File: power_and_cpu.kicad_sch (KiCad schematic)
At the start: 252 parts, among them J1 CPU1 USB, J10 AUX GPIO 1, J11 CAN2 PLUG, J12 Conn_01x06, J13 ADC AUX 2, J14 AUX GPIO 2, J15 AUX Encoder, J17 CAN Output, J2 CAN Input, J21 Power Input, J3 Encoder 1, J4 Encoder 2, J5 Conn_01x06, J6 CPU2 USB, J7 Conn_01x02, J9 ADC AUX 1, Q7 Q_NMOS_GSD, SW1 SW_MEC_5G, SW2 SW_MEC_5G, SW3 CONFIG SWITCH, U10 TXS0101DCKR, U11 TLV1117LV33DCYR, U12 W25Q128JVSIQ, U13 W25Q128JVSIQ, U15 RP2040, U16 ADC081S021CISD/NOPB, U17 isolator, U18 MCP2515-xSO, U19 RP2040, U23 SN74LVC1G07QDCKTQ1, U24 MT2492, U25 NCP1117-5_SOT223, U26 ADC081S021CISD/NOPB, U27 USBLC6-2P6, U28 USBLC6-2P6, U29 USBLC6-4SC6, U3 USBLC6-4SC6, U30 USBLC6-4SC6, U31 USBLC6-4SC6, U32 TLV1117LV33DCYR, U33 TX4139, U34 LTV-208, U43 USBLC6-4SC6, U6 SN74LVC1G07QDCKTQ1, U9 ADC081S021CISD/NOPB, Y1 12MHz, Y2 12MHz, Y3 16MHz

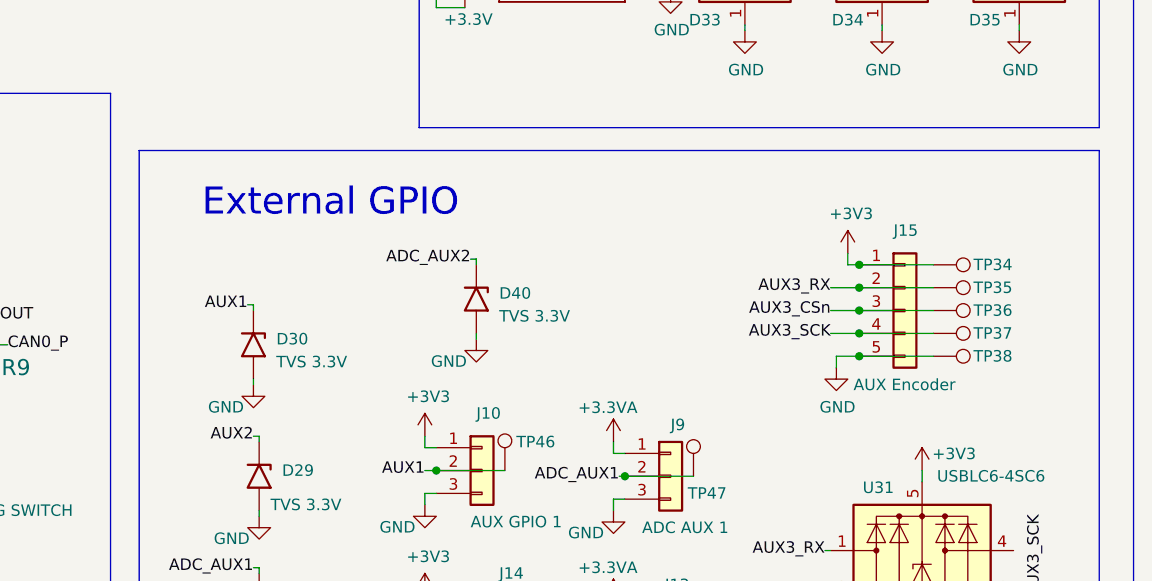
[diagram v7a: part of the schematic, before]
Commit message: Changed current sense circuit as per recommendation. Added extra combined AUX port.
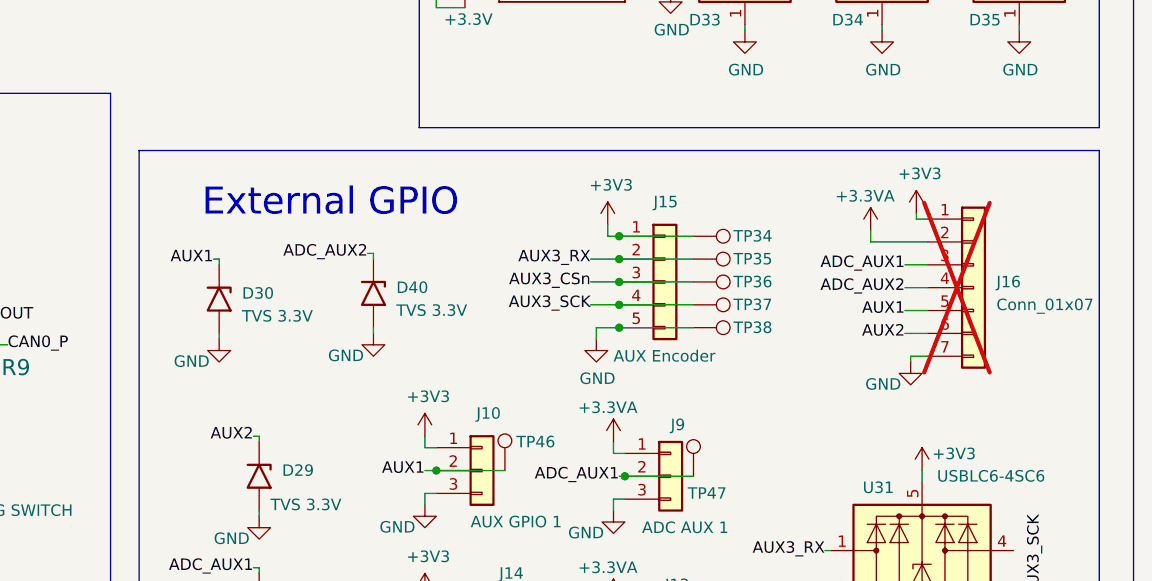
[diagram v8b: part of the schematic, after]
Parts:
- added J16: Conn_01x07, Connector_PinHeader_2.54mm:PinHeader_2x04_P2.54mm_Vertical, symbol Connector_Generic:Conn_01x07
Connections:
- net +3.3VA: now also J16.2 (Pin_2)
- net +3V3: now also J16.1 (Pin_1)
- net ADC_AUX1: now also J16.3 (Pin_3)
- net ADC_AUX2: now also J16.4 (Pin_4)
- net AUX1: now also J16.5 (Pin_5)
- net AUX2: now also J16.6 (Pin_6)
- net GND: now also J16.7 (Pin_7)
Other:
- moved on the sheet: D30, D40, J15, TP34, TP35, TP36, TP37, TP38
